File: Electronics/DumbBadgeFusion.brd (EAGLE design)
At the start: 163.5 x 113 mm, 149 parts, among them IC1 74245MTC, IC2 74245MTC, IC3 74245MTC, SW1 SPST_TACT-KMR2, T1 MMUN2133LT1G, U1 ATSAMD21J18A-AUT, U2 TPS61090RSAR, U3 MCP73871, U4 FAN5333BSX, U6 MAX3232, X4 32.768

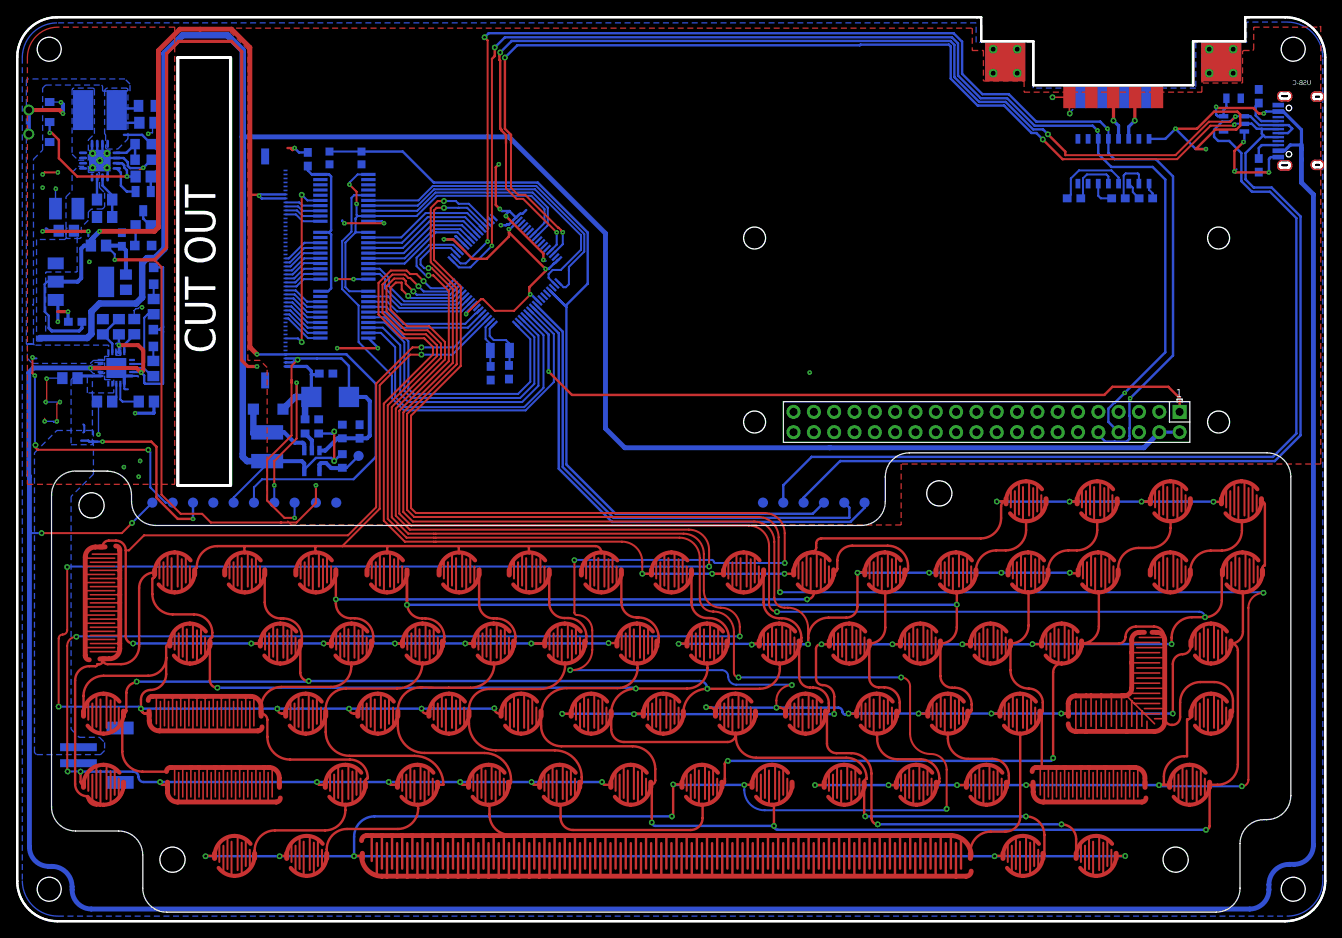
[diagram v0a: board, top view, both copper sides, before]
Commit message: almost done with keyboard
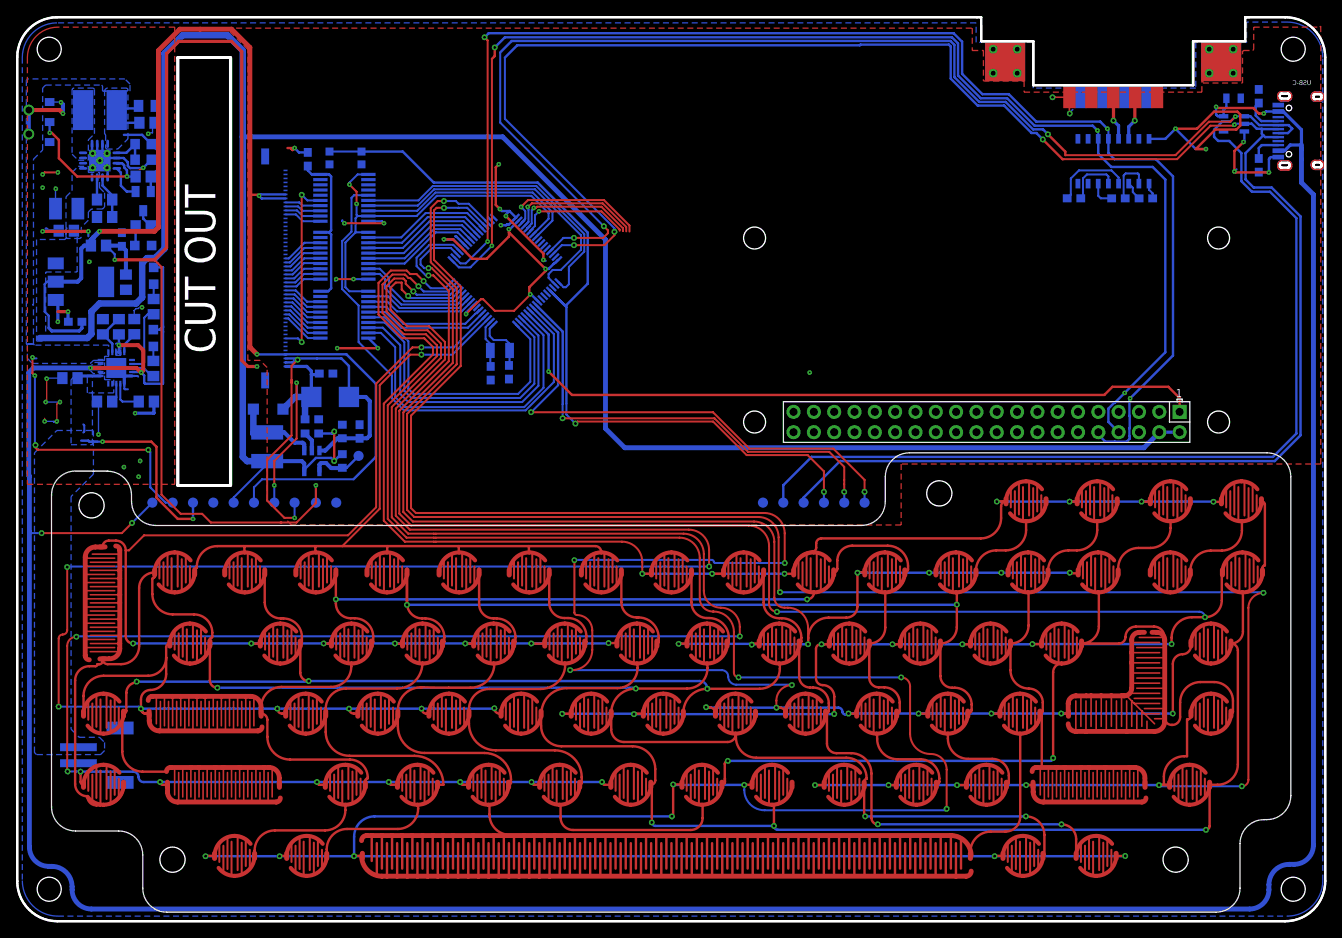
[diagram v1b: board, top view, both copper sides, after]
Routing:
- net KEYCOLUM0: track 219.3 -> 237.7 mm, vias 4 -> 5
- net KEYCOLUM1: track 206.2 -> 223.1 mm, vias 5 -> 6
- net KEYCOLUM2: track 183.6 -> 199.2 mm, vias 2 -> 3
- net KEYCOLUM3: track 191.1 -> 205.2 mm, vias 2 -> 3
- net USB_P: track 247.8 -> 255.8 mm
- net USB_N: track 258.2 -> 265.8 mm
- net SWCLK: track 62.3 -> 57.8 mm, vias 0 -> 2
- net RESET: track 107.4 -> 105.1 mm, vias 0 -> 2
- net GND: track 138.3 -> 136.7 mm
- net 5.0V: track 291.4 -> 290.8 mm
- net SWDIO: vias 0 -> 2

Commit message: ratsnest nothing to do
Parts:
- moved C22 1.42 mm to (141.2, 88.9)
- moved C23 1.42 mm to (132.2, 88.9)
- moved C24 1.42 mm to (137.7, 88.9)
- moved U6 1.42 mm to (137.1, 93.6)
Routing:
- net KEYCOLUM0: track 237.7 -> 416.6 mm, vias 5 -> 9
- net KEYCOLUM1: track 223.1 -> 381.0 mm, vias 6 -> 7
- net KEYCOLUM6: track 189.3 -> 340.2 mm, vias 3 -> 6
- net KEYCOLUM5: track 204.5 -> 350.3 mm, vias 2 -> 5
- net KEYCOLUM4: track 194.0 -> 336.2 mm, vias 0 -> 3
- net KEYCOLUM2: track 199.2 -> 331.2 mm, vias 3 -> 6
- net KEYCOLUM3: track 205.2 -> 309.6 mm
- net KEYROW7: track 260.5 -> 339.0 mm, vias 11 -> 15
- net 5.0V: track 290.8 -> 313.5 mm
- net KEYROW6: track 164.4 -> 180.3 mm, vias 8 -> 9
- net KEYROW2: track 273.2 -> 263.2 mm
- net SWDIO: track 63.8 -> 59.7 mm, vias 2 -> 0
- net KEYROW3: track 276.1 -> 272.7 mm
- net 3V3: track 230.2 -> 233.2 mm
- net KEYROW4: track 349.8 -> 346.8 mm
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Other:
- outline, holes or cut-outs redrawn

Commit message: Fixed a little bit
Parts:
- moved C24 11.0 mm to (127.5, 92.8), turned to 270 degrees
- moved C23 4.83 mm to (129.2, 92.7), turned to 270 degrees
- moved C22 3.81 mm to (144.5, 90.8)
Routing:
- net KEYCOLUM1: track 381.0 -> 404.1 mm
- net KEYCOLUM3: track 309.6 -> 332.7 mm
- net KEYCOLUM0: track 416.6 -> 439.6 mm
- net KEYCOLUM2: track 331.2 -> 353.9 mm
- net N$60: track 6.15 -> 18.2 mm
- net UART_TX: track 160.5 -> 168.2 mm
- net UART_RX: track 167.1 -> 173.9 mm
- net N$61: track 3.33 -> 9.97 mm
- net N$56: track 2.37 -> 6.60 mm
- net KEYCOLUM4: track 336.2 -> 340.1 mm
- net KEYCOLUM5: track 350.3 -> 354.0 mm
- net N$57: track 2.03 -> 5.53 mm
- net KEYCOLUM6: track 340.2 -> 343.6 mm
- net KEYROW9: track 258.8 -> 261.6 mm
- net KEYROW7: track 339.0 -> 341.6 mm
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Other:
- outline, holes or cut-outs redrawn

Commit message: updated part names
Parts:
- X4: value 32.768 -> NX3215SA-32.768K-STD-MUA-8
- renumbered DIODES to TPD3E001, U$30 to FPC50CONN

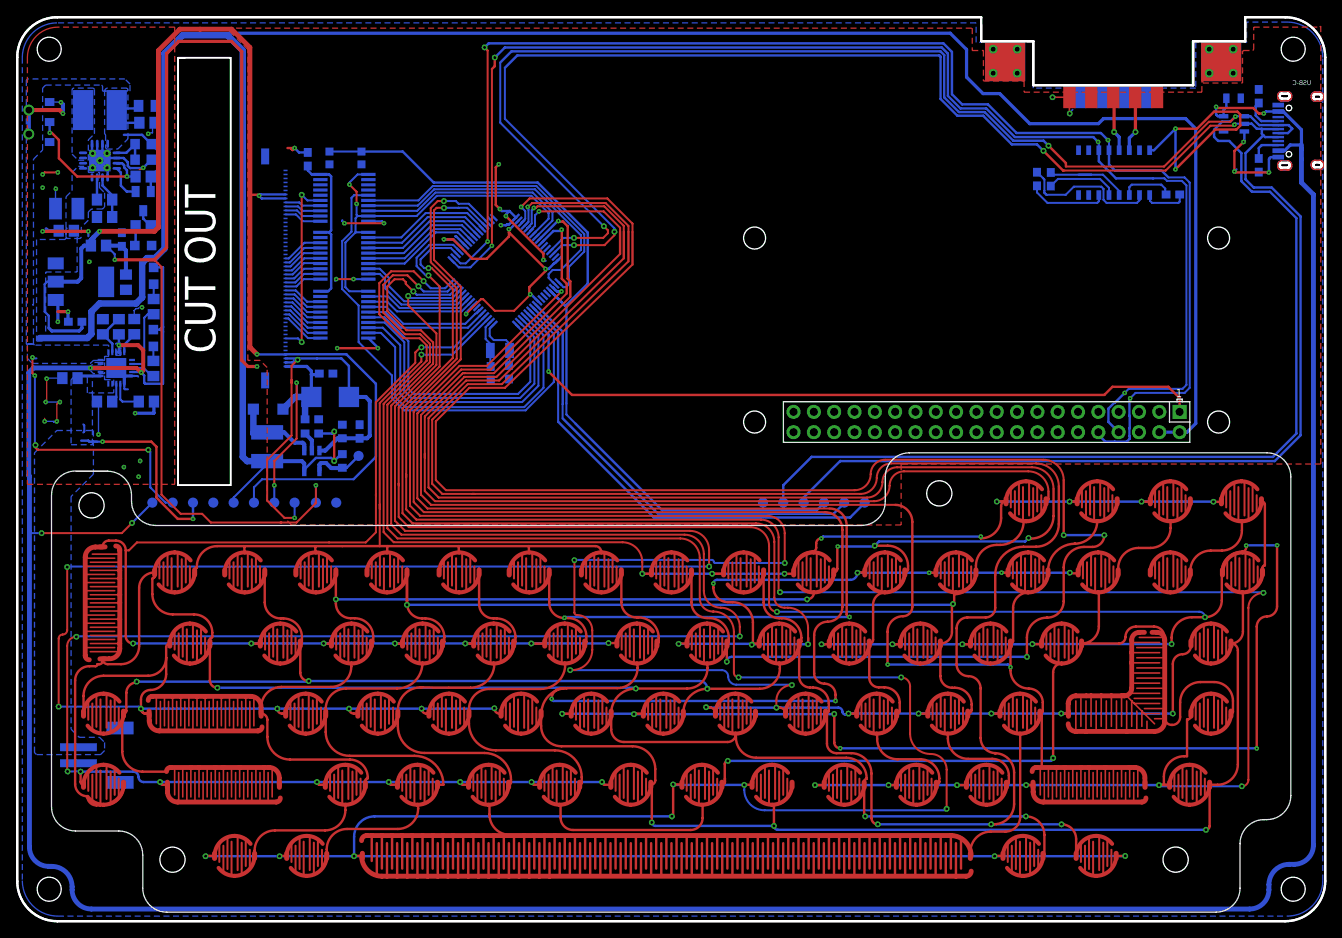
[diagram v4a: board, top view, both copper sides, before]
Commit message: Change to BOM, Macrofab order 2
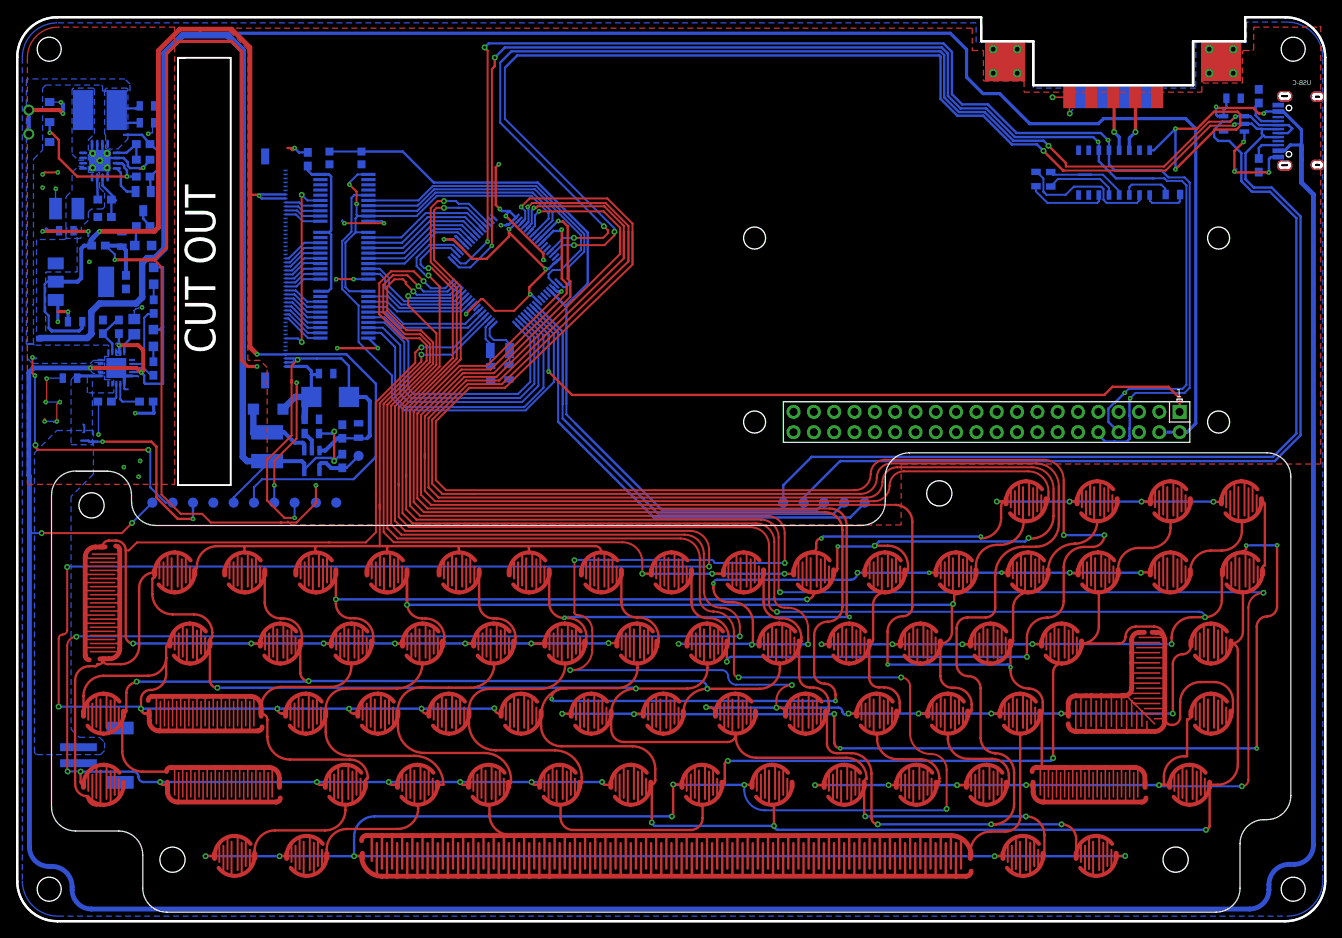
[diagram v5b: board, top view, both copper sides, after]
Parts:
- removed TP11: TPB1,27, testpad:B1,27
- C10, C11: value 1uF -> 1.0uF; device SparkFun-Capacitors:0603 -> SparkFun-Capacitors:0805
- C14, C5, C8, C9: device SparkFun-Capacitors:0603 -> SparkFun-Capacitors:0805
- C2, C3, C7: device microbuilder:0805-NO -> SparkFun-Capacitors:0805
- C22, C23, C24, C26, C27: device microbuilder:0603-NO -> SparkFun-Capacitors:0805
- C4: device microbuilder:0805_10MGAP -> SparkFun-Capacitors:0805
- LED1: value RED -> LOW BATT
- R1: device adafruit:R0603 -> SparkFun-Resistors:0603
- R10, R17: value 100K -> 100k; device microbuilder:0805-NO -> SparkFun-Resistors:0603
- R11, R14, R15, R20: value 1K -> 1k; device microbuilder:0805-NO -> SparkFun-Resistors:0603
- R12: value 6Ω -> 6 Ohm; device adafruit:R0603 -> SparkFun-Resistors:0603
- R13, R6: value 200K -> 200k; device microbuilder:0805-NO -> SparkFun-Resistors:0603
- R16: value 1.0K -> 1k; device microbuilder:0805-NO -> SparkFun-Resistors:0603
- R18: value 1.2K -> 1.2k; device microbuilder:0805-NO -> SparkFun-Resistors:0603
- R19: value 0 -> 0 Ohm
- R4: device microbuilder:0805-NO -> SparkFun-Resistors:0603
- R7: value 340K -> 340k; device microbuilder:_0805MP -> SparkFun-Resistors:0603
- R8: device microbuilder:_0805MP -> SparkFun-Resistors:0603
- R9: value 270K -> 270k; device microbuilder:0805-NO -> SparkFun-Resistors:0603
- moved C9 0.18 mm to (42.7, 61.3)
- moved C24 0.13 mm to (127.3, 92.8)
- renumbered BATT_LOW to LED2, DONE to LED3
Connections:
- net KEYROW6: now also K_BACK.P$1
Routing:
- net KEYROW6: track 182.8 -> 189.9 mm, vias 9 -> 10
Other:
- board text added: "Done"
- board text added: "LED 1"

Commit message: more stuff
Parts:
- renumbered TPD3E001 to U5
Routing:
- net KEYROW4: track 349.1 -> 356.5 mm, vias 12 -> 13
- net KEYCOLUM5: track 354.0 -> 356.8 mm
- net KEYROW9: track 261.6 -> 260.4 mm
- net KEYCOLUM3: track 332.7 -> 333.6 mm
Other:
- board text added: "Raspberry Pi Goes Here Face Down"

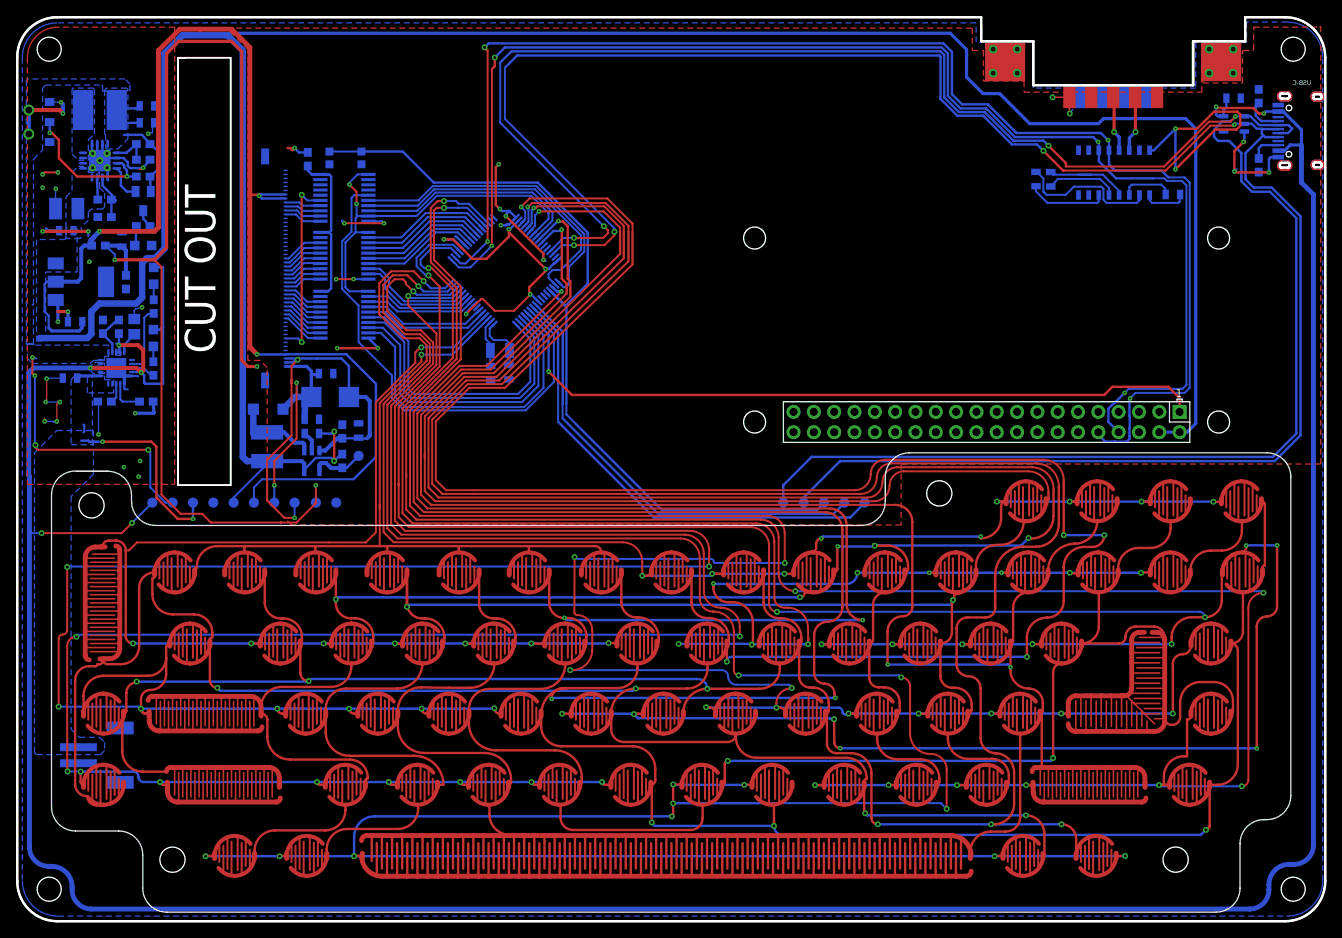
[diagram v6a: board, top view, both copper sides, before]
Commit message: created keyboard standalone, improved schematics
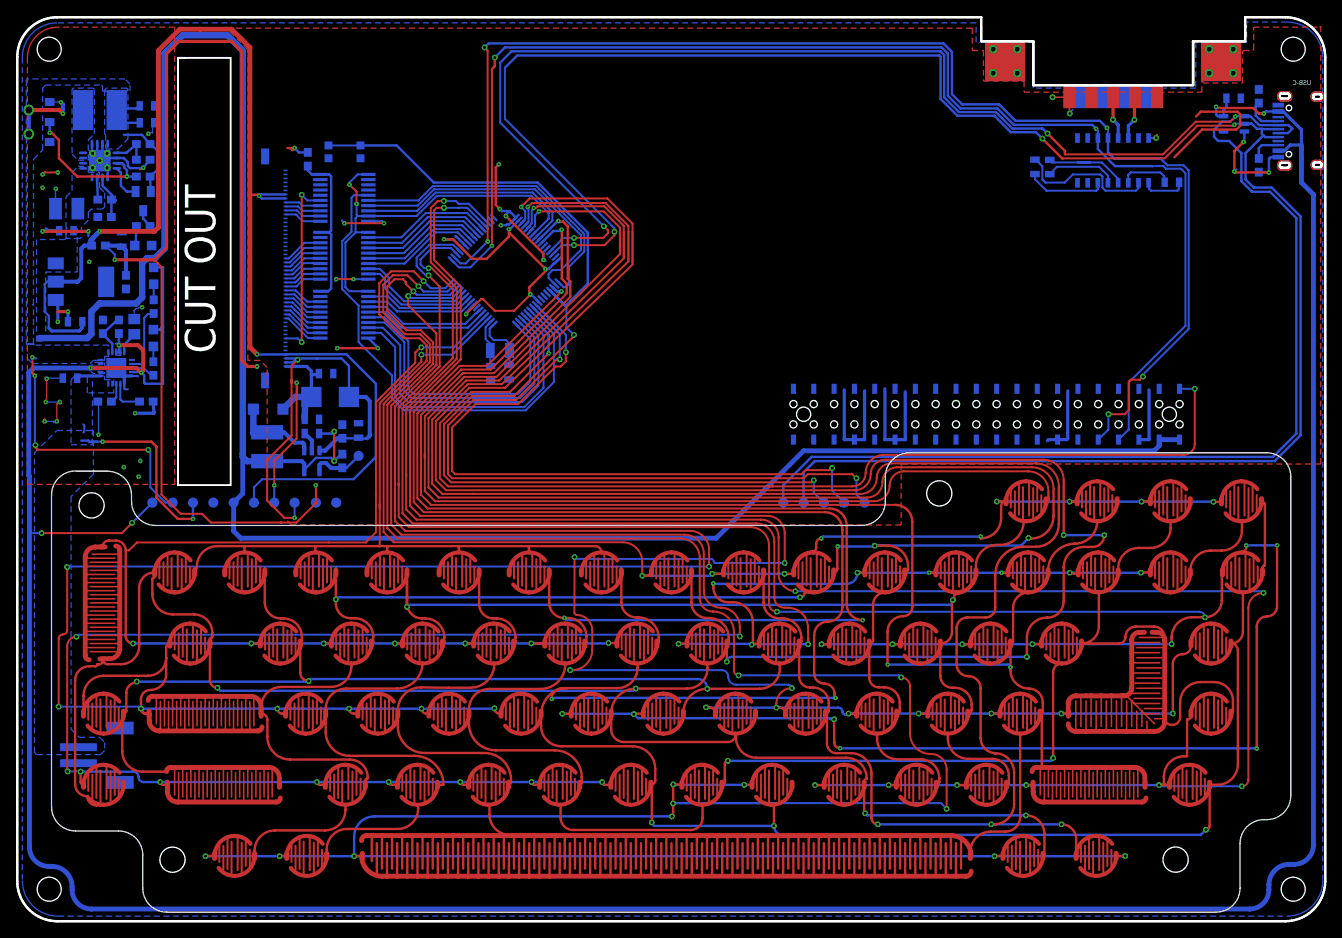
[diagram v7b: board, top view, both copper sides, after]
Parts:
- removed U$32: RPI-ZERO, RPI-Zero:RASPBERRYPI_BASTELSTUBE_V13_RASPI_BOARD_B+_FULL
- added U$30: SAMTEC_PI_REVERSE, FPC:HLE-120-02-G-DV-BE-A--REVERSEMOUNT
- moved C23 1.53 mm to (129.1, 94.3)
- moved C24 1.53 mm to (127.2, 94.3)
- moved C22 1.53 mm to (144.3, 92.4)
- moved U6 1.53 mm to (137.0, 95.1)
- moved SW1 0.77 mm to (40.9, 96.2)
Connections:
- net 5.0V: now also U$30.P2, U$30.P4; no longer U$32.2, U$32.4
- net GND: now also U$30.P14, U$30.P25, U$30.P30, U$30.P34, U$30.P39, U$30.P6, U$30.P9; no longer U$32.14, U$32.20, U$32.25, U$32.30, U$32.34, U$32.39, U$32.6, U$32.9
- net PB31: now also U$30.P1; no longer U$32.1
- net UART_RX: now also U$30.P10; no longer U$32.10
- net UART_TX: now also U$30.P8; no longer U$32.8
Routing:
- net GND: track 136.5 -> 182.3 mm
- net PB31: track 91.2 -> 136.5 mm, vias 1 -> 2
- net 5.0V: track 313.5 -> 270.7 mm
- net RESET: track 103.4 -> 134.1 mm, vias 0 -> 2
- net SWCLK: track 56.9 -> 85.7 mm, vias 0 -> 2
- net SWDIO: track 59.7 -> 86.9 mm, vias 0 -> 2
- net 3V3: track 233.3 -> 221.6 mm, vias 11 -> 10
- net KEYROW6: track 190.0 -> 194.9 mm
- net UART_RX: track 173.9 -> 169.8 mm, vias 4 -> 5
- net UART_TX: track 168.2 -> 164.8 mm, vias 4 -> 3
- net USB_P: track 255.8 -> 259.0 mm
- net N$1: track 7.06 -> 5.50 mm
- net N$52: track 7.09 -> 5.59 mm
- net USB_N: track 265.9 -> 264.7 mm
